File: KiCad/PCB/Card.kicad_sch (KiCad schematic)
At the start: 101 parts, among them J1 Conn_ST_STDC14, Q1 T2N7002AK, Q2 T2N7002AK, Q3 T2N7002AK, Q4 T2N7002AK, Q5 T2N7002AK, Q6 T2N7002AK, Q7 T2N7002AK, Q8 T2N7002AK, U2 74HC595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

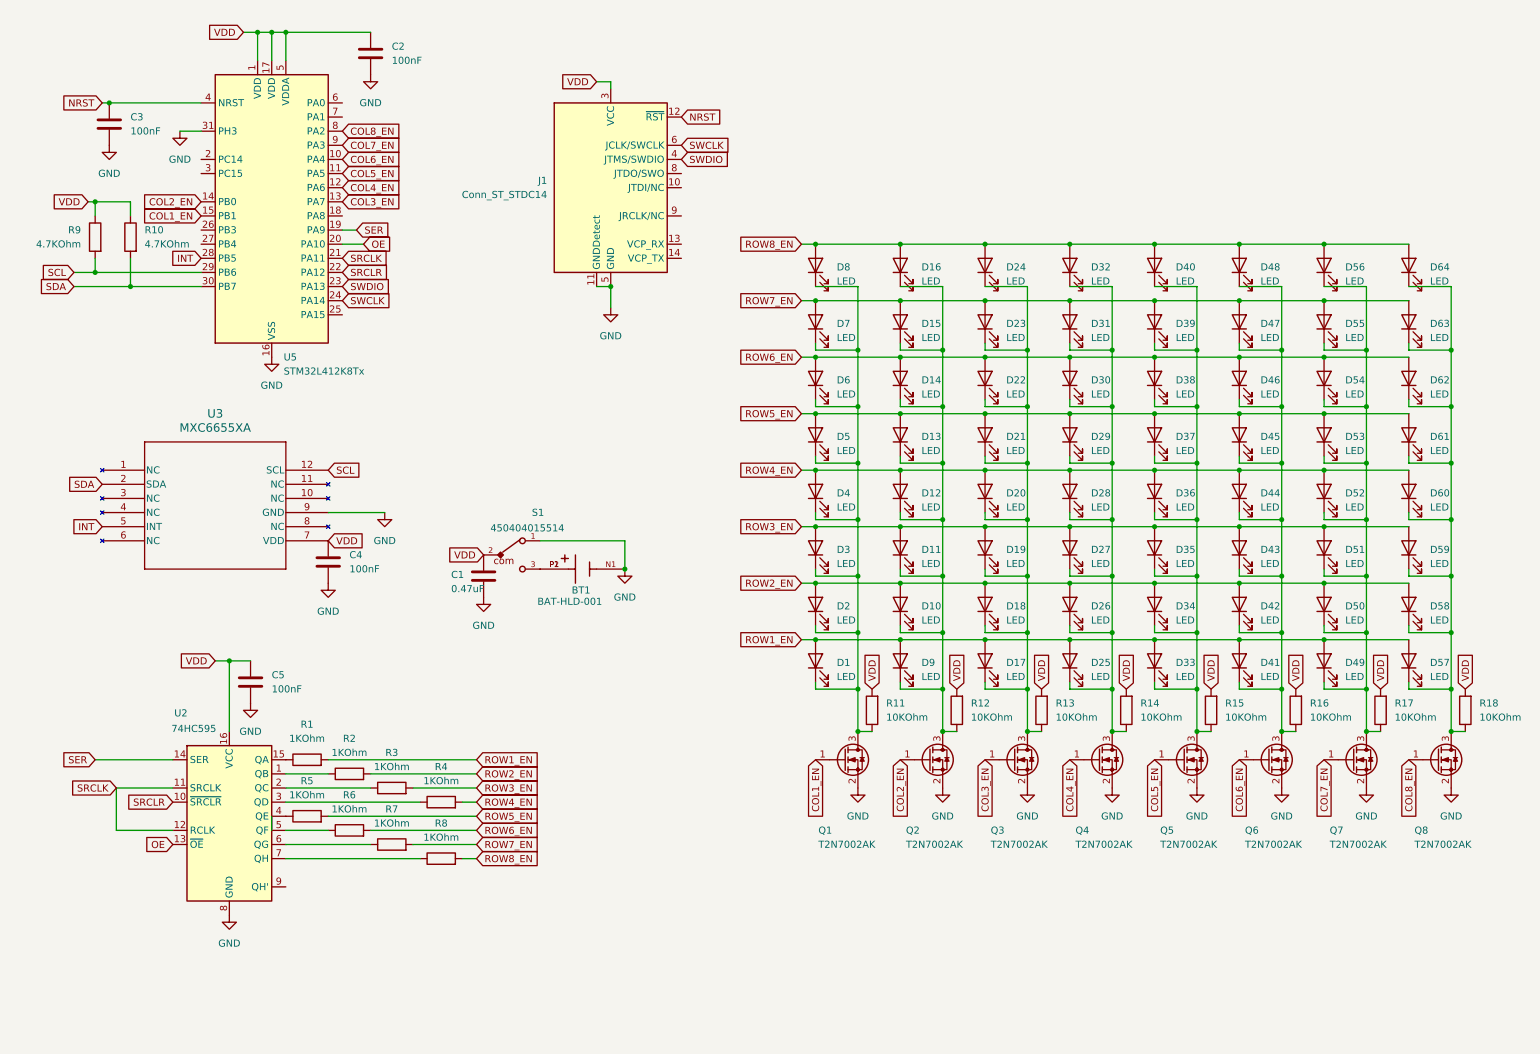
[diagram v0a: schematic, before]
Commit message: updated schematic labels
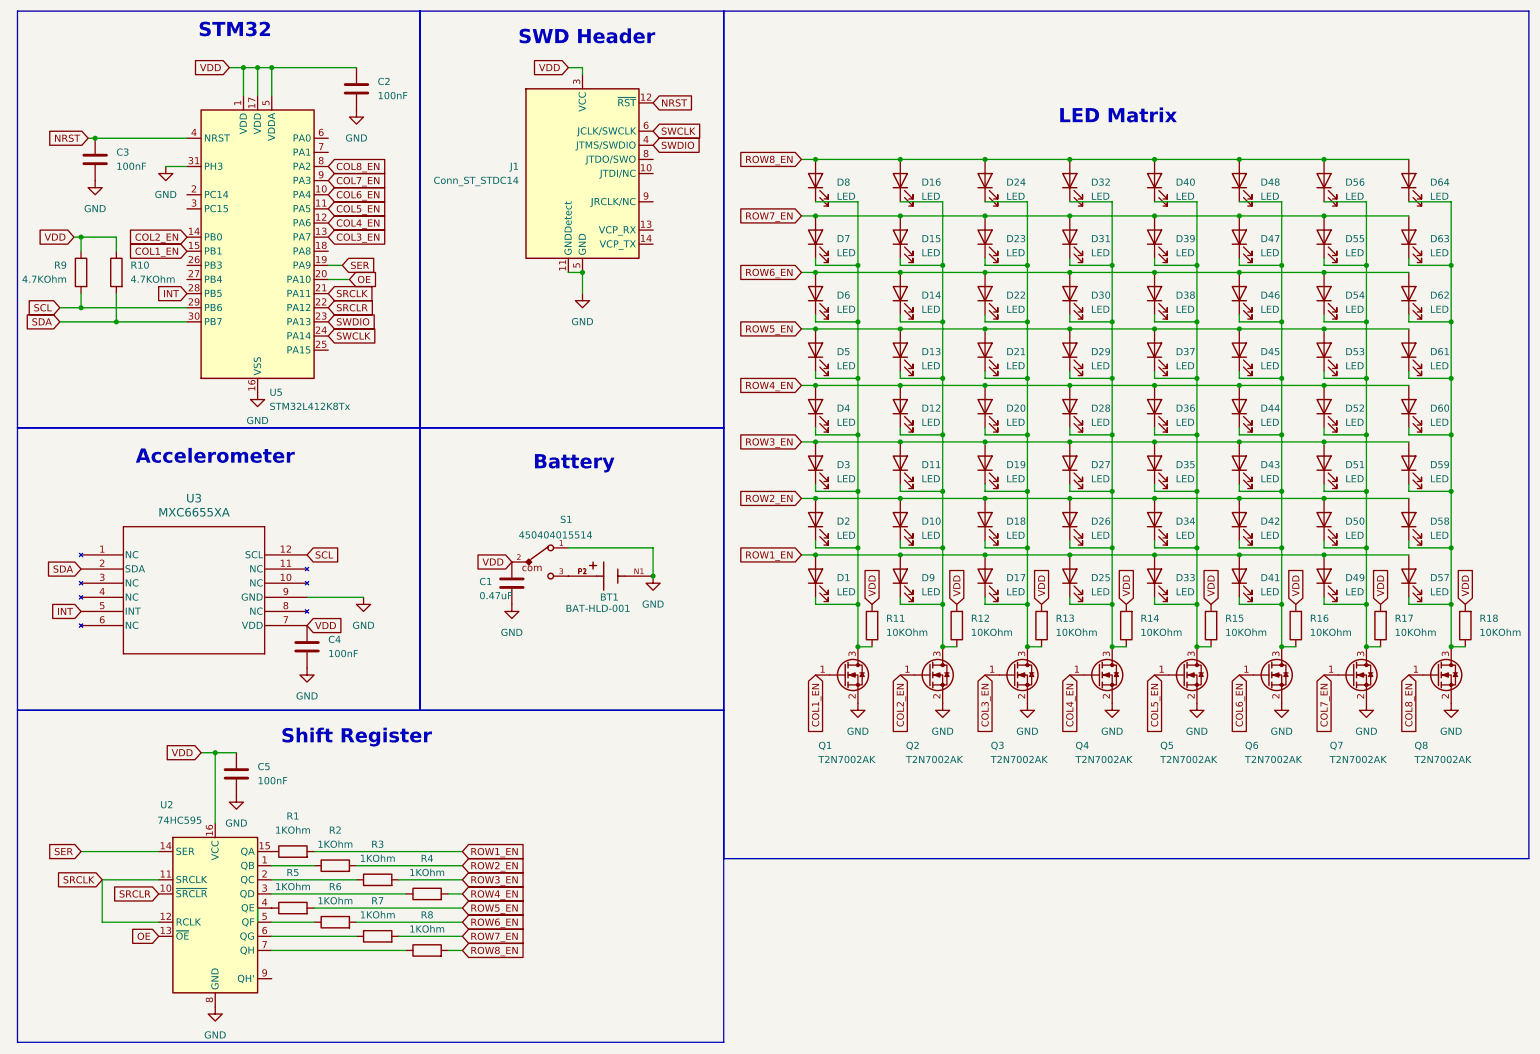
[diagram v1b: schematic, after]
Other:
- note added: "Accelerometer"
- note added: "Battery"
- note added: "LED Matrix"
- note added: "STM32"
- note added: "SWD Header"
- note added: "Shift Register"
- title: (none) -> Physics Simulating Business Card
- moved on the sheet: BT1, C1, C2, C3, C4, C5, D1, D10, D11, D12, D13, D14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
